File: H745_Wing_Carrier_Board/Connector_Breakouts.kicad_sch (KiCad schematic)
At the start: 5 parts

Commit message: Added footprints for ux
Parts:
- gave numbers to parts that had none: 5
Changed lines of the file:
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@@
   (symbol (lib_id "power:GND") (at 121.92 123.825 0) (unit 1)
     (in_bom yes) (on_board yes) (fields_autoplaced)
-    (property "Reference" "#PWR?" (id 0) (at 121.92 130.175 0)
+    (property "Reference" "#PWR0117" (id 0) (at 121.92 130.175 0)
       (effects (font (size 1.27 1.27)) hide)
     )
@@
   (symbol (lib_id "power:GND") (at 123.825 164.465 0) (unit 1)
     (in_bom yes) (on_board yes) (fields_autoplaced)
-    (property "Reference" "#PWR?" (id 0) (at 123.825 170.815 0)
+    (property "Reference" "#PWR0119" (id 0) (at 123.825 170.815 0)
       (effects (font (size 1.27 1.27)) hide)
     )
@@
   (symbol (lib_id "power:GND") (at 112.395 149.225 0) (unit 1)
     (in_bom yes) (on_board yes) (fields_autoplaced)
-    (property "Reference" "#PWR?" (id 0) (at 112.395 155.575 0)
+    (property "Reference" "#PWR0120" (id 0) (at 112.395 155.575 0)
       (effects (font (size 1.27 1.27)) hide)
     )
@@
   (symbol (lib_id "SM03B-GHS-TB_LF__SN_:SM03B-GHS-TB(LF)(SN)-") (at 139.7 104.775 0) (unit 1)
     (in_bom yes) (on_board yes) (fields_autoplaced)
-    (property "Reference" "J?" (id 0) (at 146.05 103.5049 0)
+    (property "Reference" "J10" (id 0) (at 146.05 103.5049 0)
       (effects (font (size 1.27 1.27)) (justify left))
     )
@@
   (symbol (lib_id "power:GND") (at 121.92 102.235 0) (unit 1)
     (in_bom yes) (on_board yes) (fields_autoplaced)
-    (property "Reference" "#PWR?" (id 0) (at 121.92 108.585 0)
+    (property "Reference" "#PWR0118" (id 0) (at 121.92 108.585 0)
       (effects (font (size 1.27 1.27)) hide)
     )
@@
   (symbol (lib_id "SM06B-GHS-TB_LF__SN_:SM06B-GHS-TB(LF)(SN)") (at 139.065 37.465 0) (unit 1)
     (in_bom yes) (on_board yes) (fields_autoplaced)
-    (property "Reference" "J?" (id 0) (at 144.907 37.9003 0)
+    (property "Reference" "J8" (id 0) (at 144.907 37.9003 0)
       (effects (font (size 1.27 1.27)) (justify left))
     )
@@
   (symbol (lib_id "SM03B-GHS-TB_LF__SN_:SM04B-GHS-TB(LF)(SN)-") (at 139.7 69.85 0) (unit 1)
     (in_bom yes) (on_board yes) (fields_autoplaced)
-    (property "Reference" "J?" (id 0) (at 146.685 69.8499 0)
+    (property "Reference" "J9" (id 0) (at 146.685 69.8499 0)
       (effects (font (size 1.27 1.27)) (justify left))
     )
@@
   (symbol (lib_id "power:GND") (at 112.395 64.77 0) (unit 1)
     (in_bom yes) (on_board yes) (fields_autoplaced)
-    (property "Reference" "#PWR?" (id 0) (at 112.395 71.12 0)
+    (property "Reference" "#PWR0124" (id 0) (at 112.395 71.12 0)
       (effects (font (size 1.27 1.27)) hide)
     )
@@
   (symbol (lib_id "power:GND") (at 121.92 109.855 0) (unit 1)
     (in_bom yes) (on_board yes) (fields_autoplaced)
-    (property "Reference" "#PWR?" (id 0) (at 121.92 116.205 0)
+    (property "Reference" "#PWR0113" (id 0) (at 121.92 116.205 0)
       (effects (font (size 1.27 1.27)) hide)
     )
@@
   (symbol (lib_id "power:GND") (at 121.92 131.445 0) (unit 1)
     (in_bom yes) (on_board yes) (fields_autoplaced)
-    (property "Reference" "#PWR?" (id 0) (at 121.92 137.795 0)
+    (property "Reference" "#PWR0114" (id 0) (at 121.92 137.795 0)
       (effects (font (size 1.27 1.27)) hide)
     )
@@
   (symbol (lib_id "power:+5V") (at 120.65 29.845 0) (unit 1)
     (in_bom yes) (on_board yes) (fields_autoplaced)
-    (property "Reference" "#PWR?" (id 0) (at 120.65 33.655 0)
+    (property "Reference" "#PWR0123" (id 0) (at 120.65 33.655 0)
       (effects (font (size 1.27 1.27)) hide)
     )
@@
   (symbol (lib_id "power:+9V") (at 121.92 121.285 0) (unit 1)
     (in_bom yes) (on_board yes) (fields_autoplaced)
-    (property "Reference" "#PWR?" (id 0) (at 121.92 125.095 0)
+    (property "Reference" "#PWR0116" (id 0) (at 121.92 125.095 0)
       (effects (font (size 1.27 1.27)) hide)
     )
@@
   (symbol (lib_id "power:+9V") (at 118.11 159.385 0) (unit 1)
     (in_bom yes) (on_board yes) (fields_autoplaced)
-    (property "Reference" "#PWR?" (id 0) (at 118.11 163.195 0)
+    (property "Reference" "#PWR0121" (id 0) (at 118.11 163.195 0)
       (effects (font (size 1.27 1.27)) hide)
     )
@@
   (symbol (lib_id "SM03B-GHS-TB_LF__SN_:SM03B-GHS-TB(LF)(SN)-") (at 139.7 126.365 0) (unit 1)
     (in_bom yes) (on_board yes) (fields_autoplaced)
-    (property "Reference" "J?" (id 0) (at 146.05 125.0949 0)
+    (property "Reference" "J11" (id 0) (at 146.05 125.0949 0)
       (effects (font (size 1.27 1.27)) (justify left))
     )
@@
   (symbol (lib_id "power:+9V") (at 121.92 99.695 0) (unit 1)
     (in_bom yes) (on_board yes) (fields_autoplaced)
-    (property "Reference" "#PWR?" (id 0) (at 121.92 103.505 0)
+    (property "Reference" "#PWR0115" (id 0) (at 121.92 103.505 0)
       (effects (font (size 1.27 1.27)) hide)
     )
@@
   (symbol (lib_id "power:GND") (at 120.65 47.625 0) (unit 1)
     (in_bom yes) (on_board yes) (fields_autoplaced)
-    (property "Reference" "#PWR?" (id 0) (at 120.65 53.975 0)
+    (property "Reference" "#PWR0122" (id 0) (at 120.65 53.975 0)
       (effects (font (size 1.27 1.27)) hide)
     )
@@
   (symbol (lib_id "SM06B-GHS-TB_LF__SN_:SM06B-GHS-TB(LF)(SN)") (at 139.7 154.305 0) (unit 1)
     (in_bom yes) (on_board yes) (fields_autoplaced)
-    (property "Reference" "J?" (id 0) (at 145.542 154.7403 0)
+    (property "Reference" "J12" (id 0) (at 145.542 154.7403 0)
       (effects (font (size 1.27 1.27)) (justify left))
     )
@@
   (symbol (lib_id "power:GND") (at 128.27 78.74 0) (unit 1)
     (in_bom yes) (on_board yes) (fields_autoplaced)
-    (property "Reference" "#PWR?" (id 0) (at 128.27 85.09 0)
-      (effects (font (size 1.27 1.27)) hide)
-    )
+    (property "Reference" "#PWR0125" (id 0) (at 128.27 85.09 0)
+      (effects (font (size 1.27 1.27)) hide)
+    )

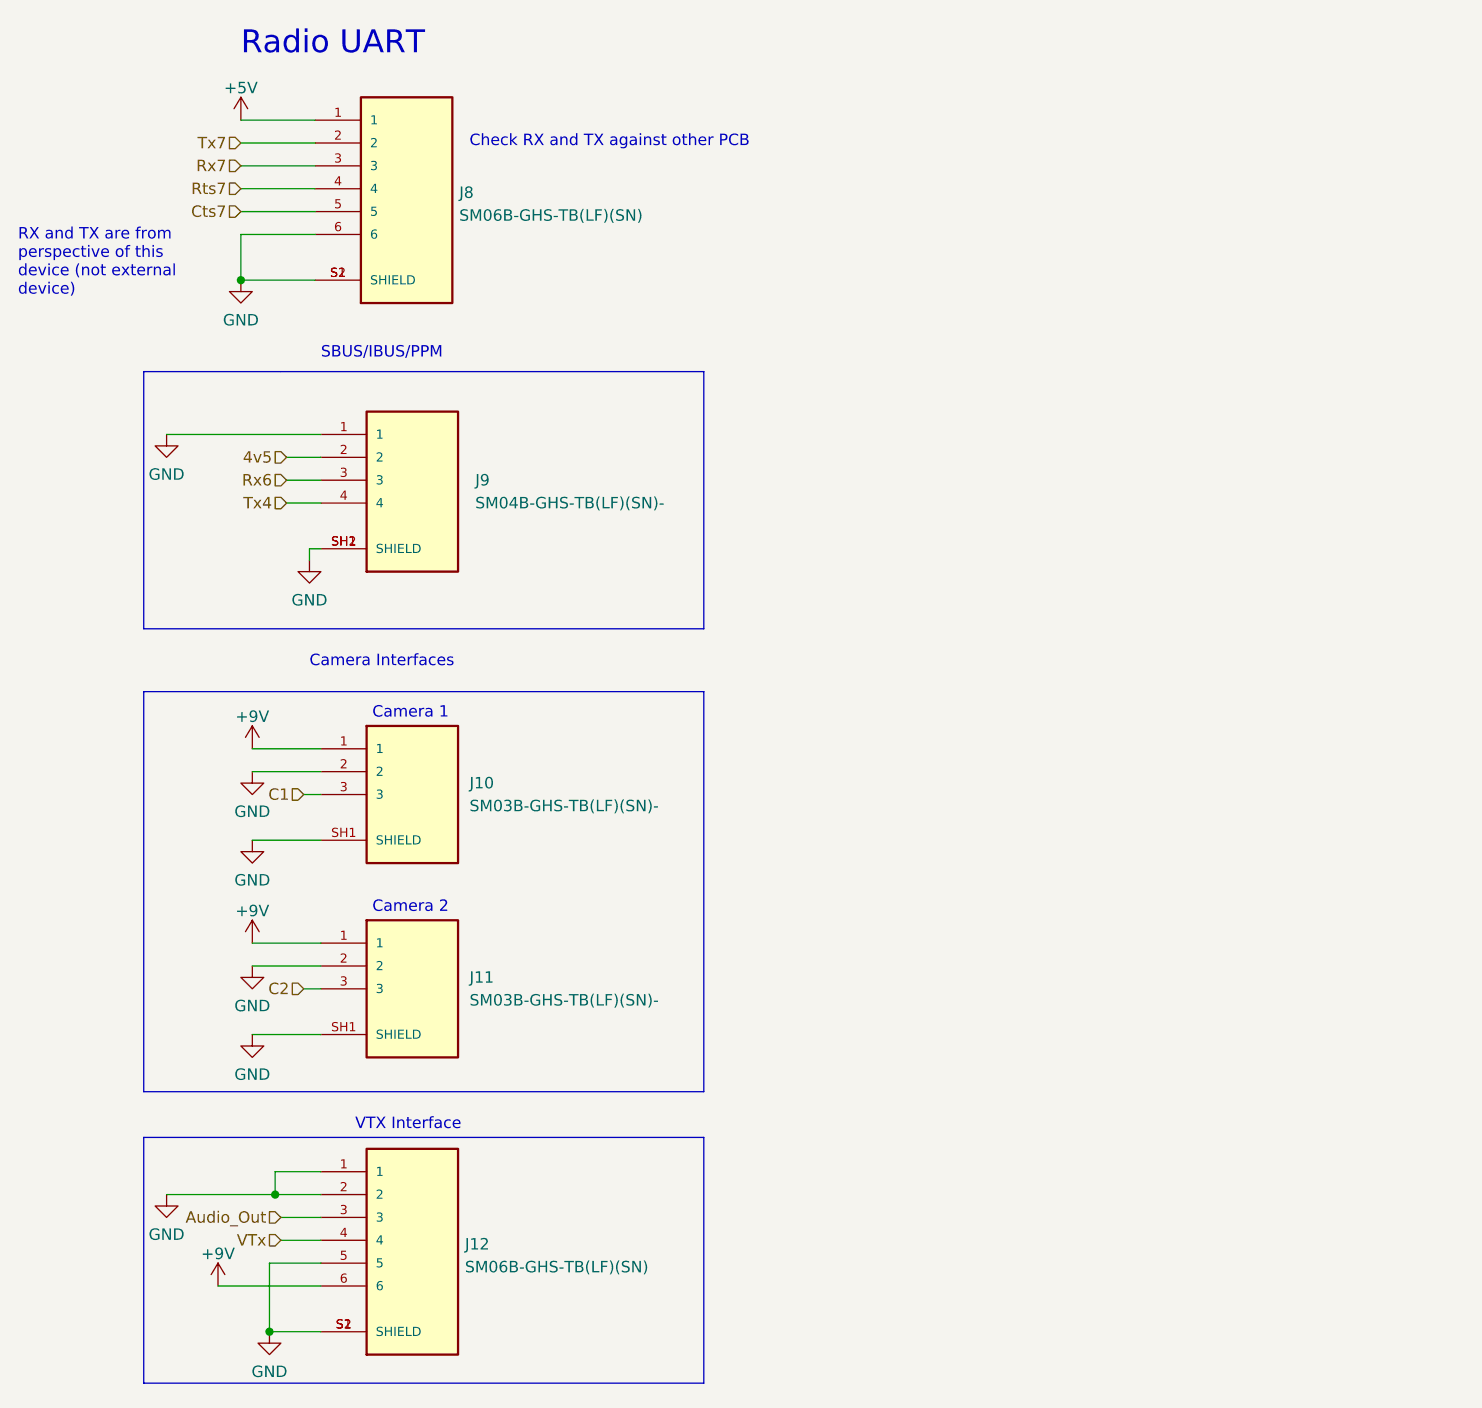
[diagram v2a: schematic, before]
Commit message: Traced together some stuff:
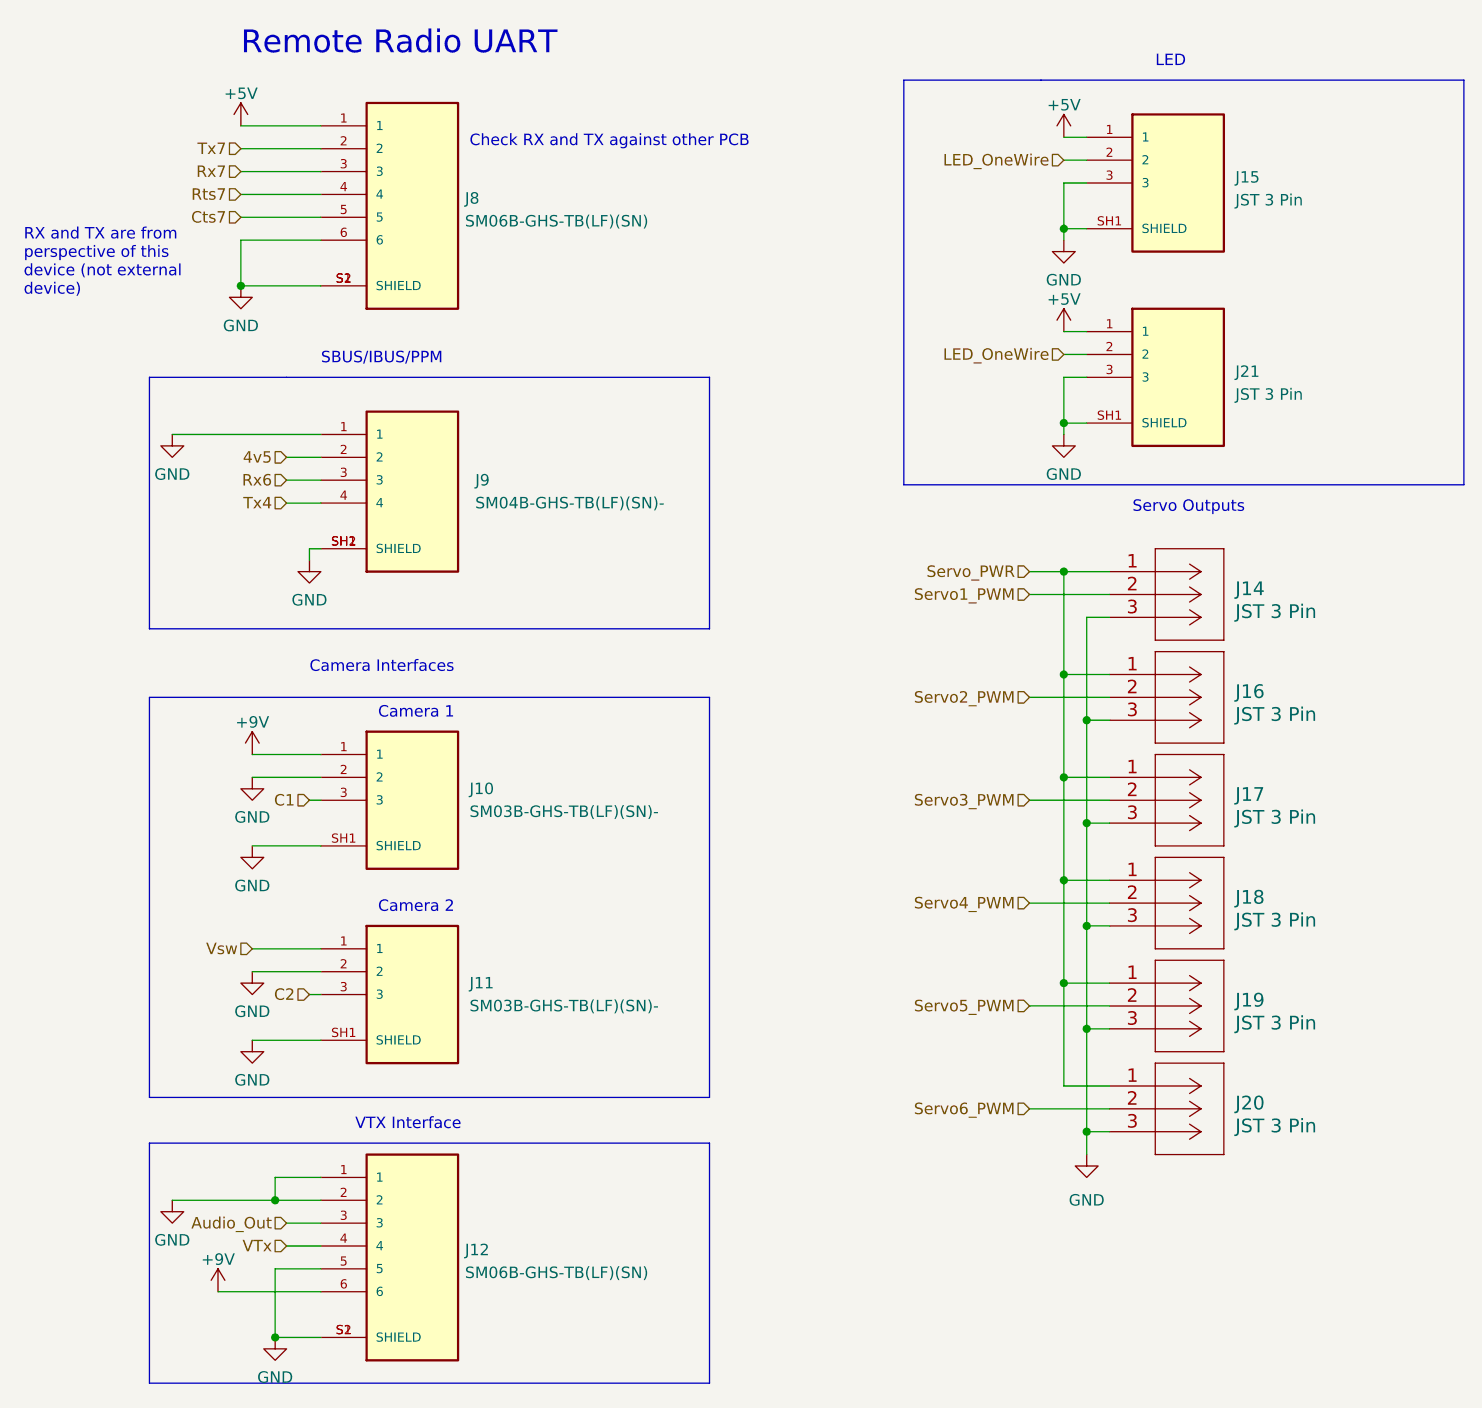
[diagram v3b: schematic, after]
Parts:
- added J14, J16, J17, J18, J19, J20: JST 3 Pin, Connector_JST:JST_XH_B3B-XH-A_1x03_P2.50mm_Vertical, symbol SM03B-PASS-1-TBTLFSN:SM03B-PASS-1-TBTLFSN
- added J15, J21: JST 3 Pin, Connector_JST:JST_XH_B3B-XH-A_1x03_P2.50mm_Vertical, symbol SM03B-GHS-TB_LF__SN_:SM03B-GHS-TB(LF)(SN)-
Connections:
- net +5V: now also J15.1, J21.1
- net +9V: no longer J11.1
- net GND: now also J14.3, J15.3, J15.SH1 (SHIELD), J16.3, J17.3, J18.3, J19.3, J20.3, J21.3, J21.SH1 (SHIELD)
- new net LED_OneWire: J15.2, J21.2
- new net Servo1_PWM: J14.2
- new net Servo2_PWM: J16.2
- new net Servo3_PWM: J17.2
- new net Servo4_PWM: J18.2
- new net Servo5_PWM: J19.2
- new net Servo6_PWM: J20.2
- new net Servo_PWR: J14.1, J16.1, J17.1, J18.1, J19.1, J20.1
- new net Vsw: J11.1
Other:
- note added: "LED"
- note added: "Remote Radio UART"
- note added: "Servo Outputs"
- note removed: "Radio UART"
- moved on the sheet: J10, J11, J12, J8
